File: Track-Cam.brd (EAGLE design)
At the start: 65 x 56 mm, 40 parts, among them IC1 STM32F042K6T, IC2 BD6211F, IC3 BD6211F, Q1 8MHz, X1 RASPI_BOARD_B+#_HC

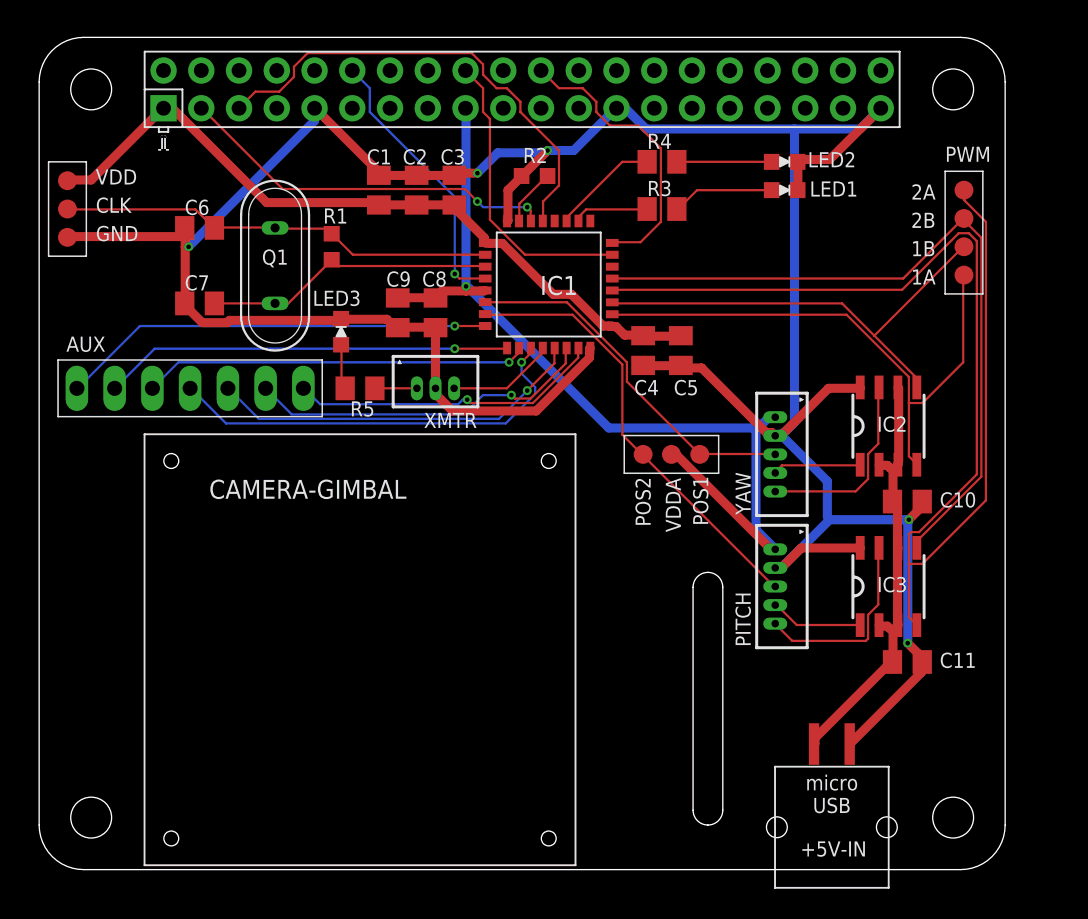
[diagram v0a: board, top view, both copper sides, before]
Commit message: enlarge pads
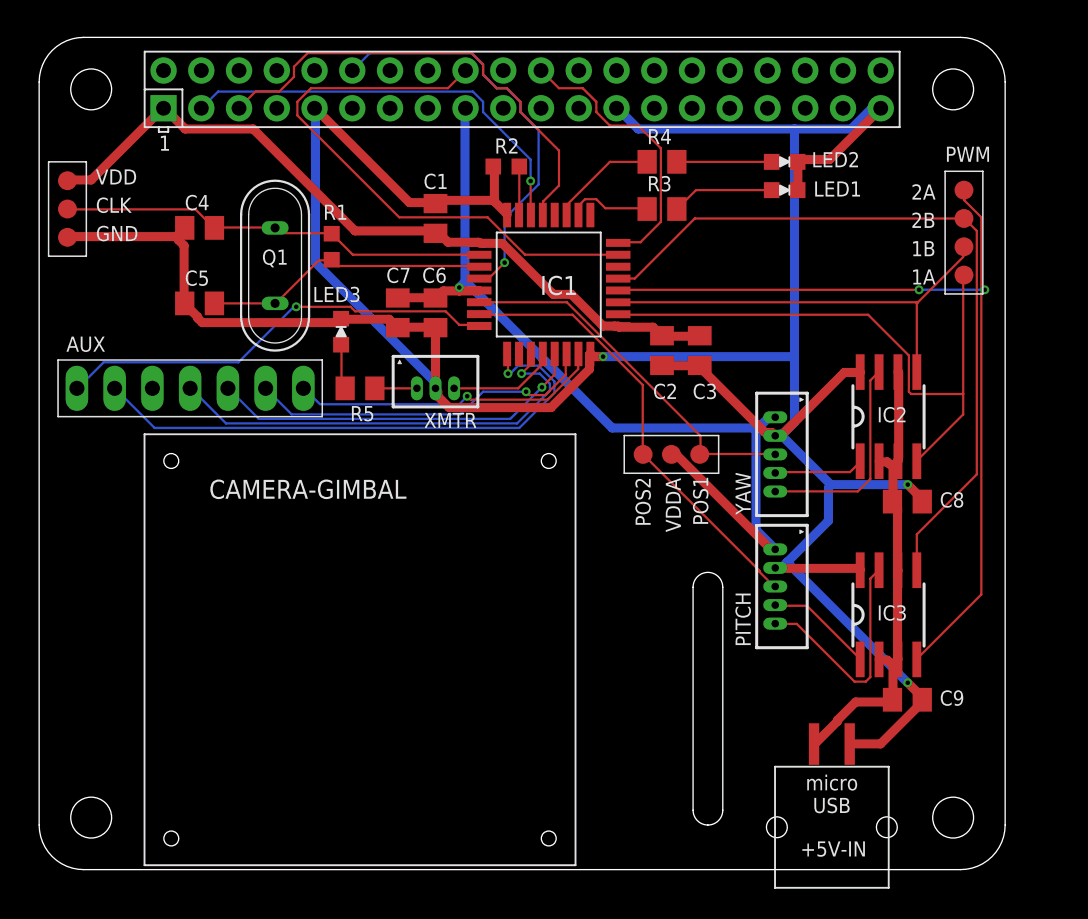
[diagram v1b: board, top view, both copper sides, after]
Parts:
- removed C10, C11: 10μ, gen-discrete:SMD2012
- C2: value 4.7μ -> 0.1μ
- C3: value 0.1μ -> 4.7μ
- C4: value 0.1μ -> 20p
- C5: value 4.7μ -> 20p
- C6: value 20p -> 10n
- C7: value 20p -> 1μ
- C9: value 1μ -> 10μ
- IC1: value STM32F042K6T -> STM32F042KT/M; device stm32:LQFP32 -> stm32:LQFP32-M
- IC2, IC3: value BD6211F -> BD6211F/M; device rohm-modified:SOP8 -> rohm-modified:SOP8/M
- moved C9 43.1 mm to (58.4, 11.4), turned to 0 degrees
- moved C8 34.2 mm to (58.4, 24.8), turned to 0 degrees
- moved C5 32.5 mm to (10.8, 38.1), turned to 0 degrees
- moved C4 31.0 mm to (10.8, 43.2), turned to 0 degrees
- moved C3 19.7 mm to (44.5, 34.9), turned to 270 degrees
- moved C2 19.7 mm to (41.9, 34.9), turned to 270 degrees
- moved C6 16.9 mm to (26.7, 37.5), turned to 270 degrees
- moved C7 13.4 mm to (24.1, 37.5), turned to 270 degrees
- moved C1 4.26 mm to (26.7, 43.8)
- moved R2 2.01 mm to (31.4, 47.3)
- moved IC3 1.91 mm to (57.1, 17.1)
- moved IC2 0.64 mm to (57.1, 30.5)
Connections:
- net PA2 renamed N$1
- net PA3 renamed N$2
- net PA5 renamed N$4
- net PA7 renamed N$5
- net PB0 renamed N$6
- net PB1 renamed N$7
- removed net PA4: AUX.3, IC1.10
- new net N$3: IC1.10
- net +3V3: now also C6.1, C7.1; no longer C8.1, C9.1
- net +5V: now also C8.1, C9.1; no longer C10.1, C11.1
- net GND: now also C4.1, C5.1, C6.2, C7.2; no longer C10.2, C11.2, C4.2, C5.2, C6.1, C7.1
- net OSC_IN: now also C4.2; no longer C6.2
- net OSC_OUT: now also C5.2; no longer C7.2
- net VDD: no longer C4.1, C5.1
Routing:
- net PA4: track 26.0 -> 0.00 mm, vias 1 -> 0
- net MOTOR2_F: track 83.1 -> 58.8 mm, vias 0 -> 2
- net SWDIO: track 19.9 -> 38.6 mm
- net GND: track 202.4 -> 213.5 mm, vias 5 -> 3
- net N$2: track 27.5 -> 37.6 mm
- net NRST: track 19.0 -> 28.0 mm
- net SDA: track 25.7 -> 28.7 mm, vias 2 -> 1
- net +5V: track 28.9 -> 31.2 mm
- net MOTOR2-: track 13.2 -> 15.6 mm
- net MOTOR1_F: track 38.5 -> 40.8 mm
- net MOTOR1_R: track 31.7 -> 29.9 mm
- net N$4: track 28.7 -> 30.3 mm
- net MOTOR1-: track 13.1 -> 14.2 mm
- net VDD: track 49.9 -> 50.9 mm
- net MOTOR2+: track 6.31 -> 7.27 mm
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
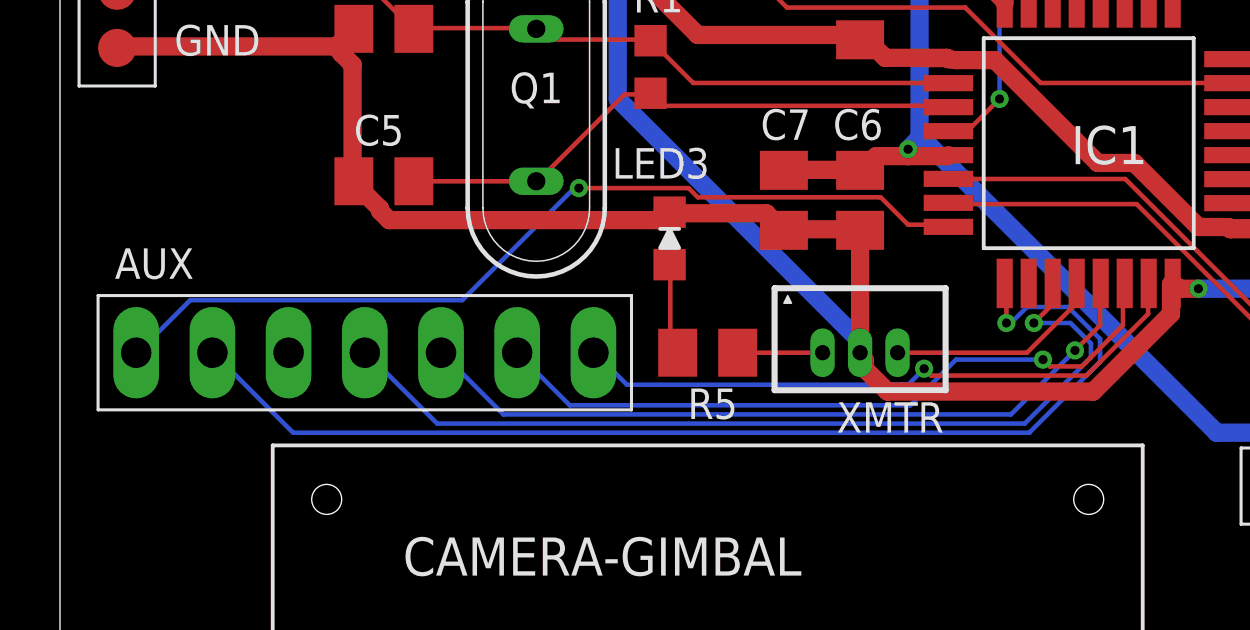
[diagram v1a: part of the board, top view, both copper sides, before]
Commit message: fix issue of unconnected path
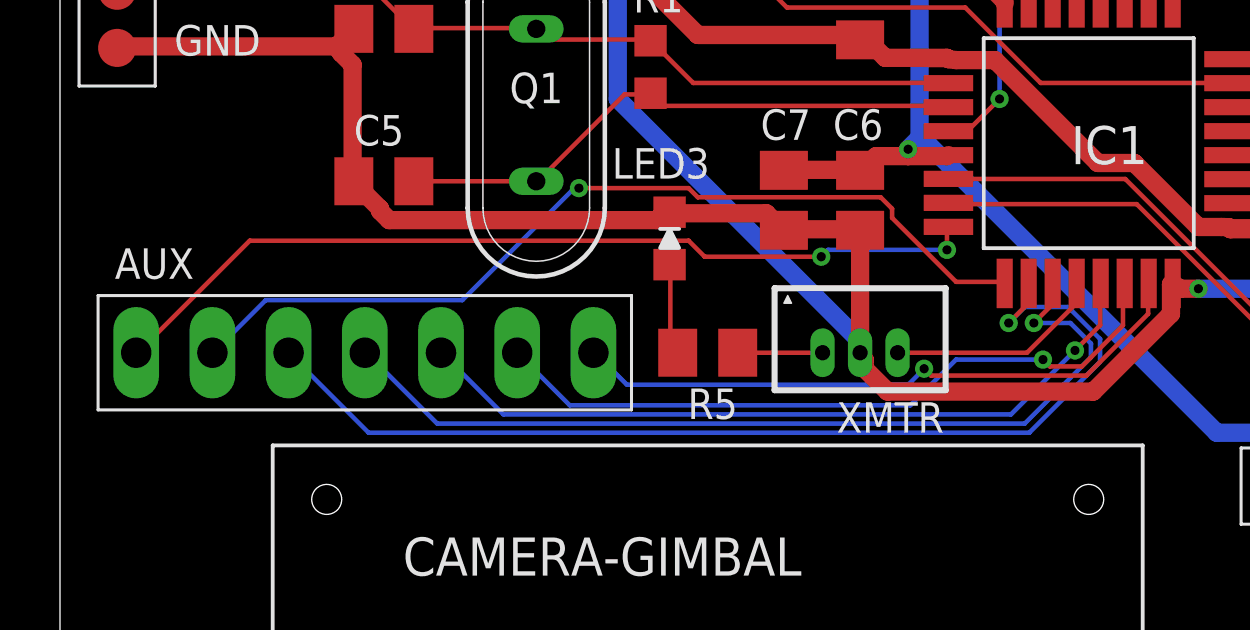
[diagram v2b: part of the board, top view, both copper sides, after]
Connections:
- net N$3: now also AUX.3
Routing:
- net N$3: track 0.00 -> 35.2 mm, vias 0 -> 1
- net N$2: track 37.6 -> 30.2 mm
- net N$1: track 29.9 -> 29.7 mm, vias 1 -> 2
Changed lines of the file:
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@@
 <contactref element="IC1" pad="8"/>
 <contactref element="AUX" pad="1"/>
-<wire x1="28.2702" y1="36.6522" x2="29.5656" y2="36.6522" width="0.1524" layer="1"/>
-<wire x1="27.3558" y1="37.5666" x2="28.2702" y2="36.6522" width="0.1524" layer="1"/>
+<wire x1="29.5656" y1="35.814" x2="29.5656" y2="36.576" width="0.1524" layer="1"/>
+<wire x1="25.6032" y1="35.814" x2="29.5656" y2="35.814" width="0.1524" layer="16"/>
+<wire x1="25.3746" y1="35.5854" x2="25.6032" y2="35.814" width="0.1524" layer="16"/>
+<wire x1="21.4884" y1="35.5854" x2="25.3746" y2="35.5854" width="0.1524" layer="1"/>
+<wire x1="20.955" y1="36.1188" x2="21.4884" y2="35.5854" width="0.1524" layer="1"/>
+<wire x1="6.3246" y1="36.1188" x2="20.955" y2="36.1188" width="0.1524" layer="1"/>
+<wire x1="2.5908" y1="32.385" x2="6.3246" y2="36.1188" width="0.1524" layer="1"/>
+<wire x1="29.5656" y1="36.576" x2="29.615" y2="36.58" width="0.1524" layer="1"/>
+<wire x1="2.5908" y1="32.385" x2="2.54" y2="32.385" width="0.1524" layer="1"/>
+<via x="29.5656" y="35.814" extent="1-16" drill="0.3048"/>
+<via x="25.3746" y="35.5854" extent="1-16" drill="0.3048"/>
+</signal>
+<signal name="N$2">
+<contactref element="IC1" pad="9"/>
+<contactref element="AUX" pad="2"/>
+<wire x1="29.8704" y1="34.7472" x2="31.4706" y2="34.7472" width="0.1524" layer="1"/>
+<wire x1="27.7368" y1="36.8808" x2="29.8704" y2="34.7472" width="0.1524" layer="1"/>
+<wire x1="27.7368" y1="37.1856" x2="27.7368" y2="36.8808" width="0.1524" layer="1"/>
+<wire x1="27.3558" y1="37.5666" x2="27.7368" y2="37.1856" width="0.1524" layer="1"/>
 <wire x1="21.2598" y1="37.5666" x2="27.3558" y2="37.5666" width="0.1524" layer="1"/>
 <wire x1="20.955" y1="37.8714" x2="21.2598" y2="37.5666" width="0.1524" layer="1"/>
@@
 <wire x1="17.145" y1="37.8714" x2="17.2974" y2="37.8714" width="0.1524" layer="16"/>
 <wire x1="13.4112" y1="34.1376" x2="17.145" y2="37.8714" width="0.1524" layer="16"/>
-<wire x1="4.3434" y1="34.1376" x2="13.4112" y2="34.1376" width="0.1524" layer="16"/>
-<wire x1="2.5908" y1="32.385" x2="4.3434" y2="34.1376" width="0.1524" layer="16"/>
-<wire x1="29.5656" y1="36.6522" x2="29.615" y2="36.58" width="0.1524" layer="1"/>
-<wire x1="2.5908" y1="32.385" x2="2.54" y2="32.385" width="0.1524" layer="16"/>
+<wire x1="6.858" y1="34.1376" x2="13.4112" y2="34.1376" width="0.1524" layer="16"/>
+<wire x1="5.1054" y1="32.385" x2="6.858" y2="34.1376" width="0.1524" layer="16"/>
+<wire x1="31.4706" y1="34.7472" x2="31.49" y2="34.695" width="0.1524" layer="1"/>
+<wire x1="5.1054" y1="32.385" x2="5.08" y2="32.385" width="0.1524" layer="16"/>
 <via x="17.2974" y="37.8714" extent="1-16" drill="0.3048"/>
-</signal>
-<signal name="N$2">
-<contactref element="IC1" pad="9"/>
-<contactref element="AUX" pad="2"/>
-<wire x1="31.5468" y1="33.3756" x2="31.5468" y2="34.671" width="0.1524" layer="1"/>
-<wire x1="31.6992" y1="33.3756" x2="31.5468" y2="33.3756" width="0.1524" layer="16"/>
-<wire x1="32.2326" y1="33.909" x2="31.6992" y2="33.3756" width="0.1524" layer="16"/>
-<wire x1="33.6042" y1="33.909" x2="32.2326" y2="33.909" width="0.1524" layer="16"/>
-<wire x1="34.671" y1="32.8422" x2="33.6042" y2="33.909" width="0.1524" layer="16"/>
-<wire x1="34.671" y1="32.0802" x2="34.671" y2="32.8422" width="0.1524" layer="16"/>
-<wire x1="32.3088" y1="29.718" x2="34.671" y2="32.0802" width="0.1524" layer="16"/>
-<wire x1="7.7724" y1="29.718" x2="32.3088" y2="29.718" width="0.1524" layer="16"/>
-<wire x1="5.1054" y1="32.385" x2="7.7724" y2="29.718" width="0.1524" layer="16"/>
-<wire x1="31.5468" y1="34.671" x2="31.49" y2="34.695" width="0.1524" layer="1"/>
-<wire x1="5.1054" y1="32.385" x2="5.08" y2="32.385" width="0.1524" layer="16"/>
-<via x="31.5468" y="33.3756" extent="1-16" drill="0.3048"/>
-</signal>
-<signal name="N$3">
-<contactref element="IC1" pad="10"/>
 </signal>
 <signal name="N$4">
@@
 <via x="28.8036" y="31.8516" extent="1-16" drill="0.3048"/>
 </signal>
+<signal name="N$3">
+<contactref element="IC1" pad="10"/>
+<contactref element="AUX" pad="3"/>
+<wire x1="32.2326" y1="33.9852" x2="32.2326" y2="34.671" width="0.1524" layer="1"/>
+<wire x1="31.623" y1="33.3756" x2="32.2326" y2="33.9852" width="0.1524" layer="1"/>
+<wire x1="32.1564" y1="33.909" x2="31.623" y2="33.3756" width="0.1524" layer="16"/>
+<wire x1="33.6042" y1="33.909" x2="32.1564" y2="33.909" width="0.1524" layer="16"/>
+<wire x1="34.671" y1="32.8422" x2="33.6042" y2="33.909" width="0.1524" layer="16"/>
+<wire x1="34.671" y1="32.0802" x2="34.671" y2="32.8422" width="0.1524" layer="16"/>
+<wire x1="32.3088" y1="29.718" x2="34.671" y2="32.0802" width="0.1524" layer="16"/>
+<wire x1="10.287" y1="29.718" x2="32.3088" y2="29.718" width="0.1524" layer="16"/>
+<wire x1="7.62" y1="32.385" x2="10.287" y2="29.718" width="0.1524" layer="16"/>
+<wire x1="32.2326" y1="34.671" x2="32.29" y2="34.695" width="0.1524" layer="1"/>
+<via x="31.623" y="33.3756" extent="1-16" drill="0.3048"/>
+</signal>
 </signals>

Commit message: add polygon net
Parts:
- +5V-IN: value MRUSB-2B-D14NI-S306 -> MRUSB-2B-D14NI-S306/M; device connector:MICRO-USB-POWER -> connector:MICRO-USB-POWER/M
- moved C8 1.91 mm to (56.5, 24.8), turned to 180 degrees
- moved C9 1.91 mm to (56.5, 11.4), turned to 180 degrees
- moved CLK 1.91 mm to (3.81, 44.5)
- moved GND 1.91 mm to (3.81, 42.5)
- moved VDD 1.91 mm to (3.81, 46.4)
- renumbered Q1 to XT1
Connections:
- net N$1 renamed PA2
- net N$2 renamed PA3
- net N$3 renamed PA4
- net N$4 renamed PA5
- net N$5 renamed PA7
- net N$6 renamed PB0
- net N$7 renamed PB1
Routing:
- net GND: track 213.5 -> 188.2 mm, vias 3 -> 10
- net VDD: track 50.9 -> 42.4 mm
- net MOTOR2_R: track 50.7 -> 55.9 mm
- net +5V: track 31.2 -> 35.0 mm
- net OSC_IN: track 29.0 -> 27.1 mm
- net MOTOR2_F: track 58.8 -> 60.6 mm, vias 2 -> 0
- net +3V3: vias 1 -> 3
- added copper zone on layer 1, net +3V3
- added copper zone on layer 16, net +3V3
- added copper zone on layer 1, net +5V
- added copper zone on layer 1, net GND
- added copper zone on layer 16, net GND
- added copper zone on layer 1, net VDD

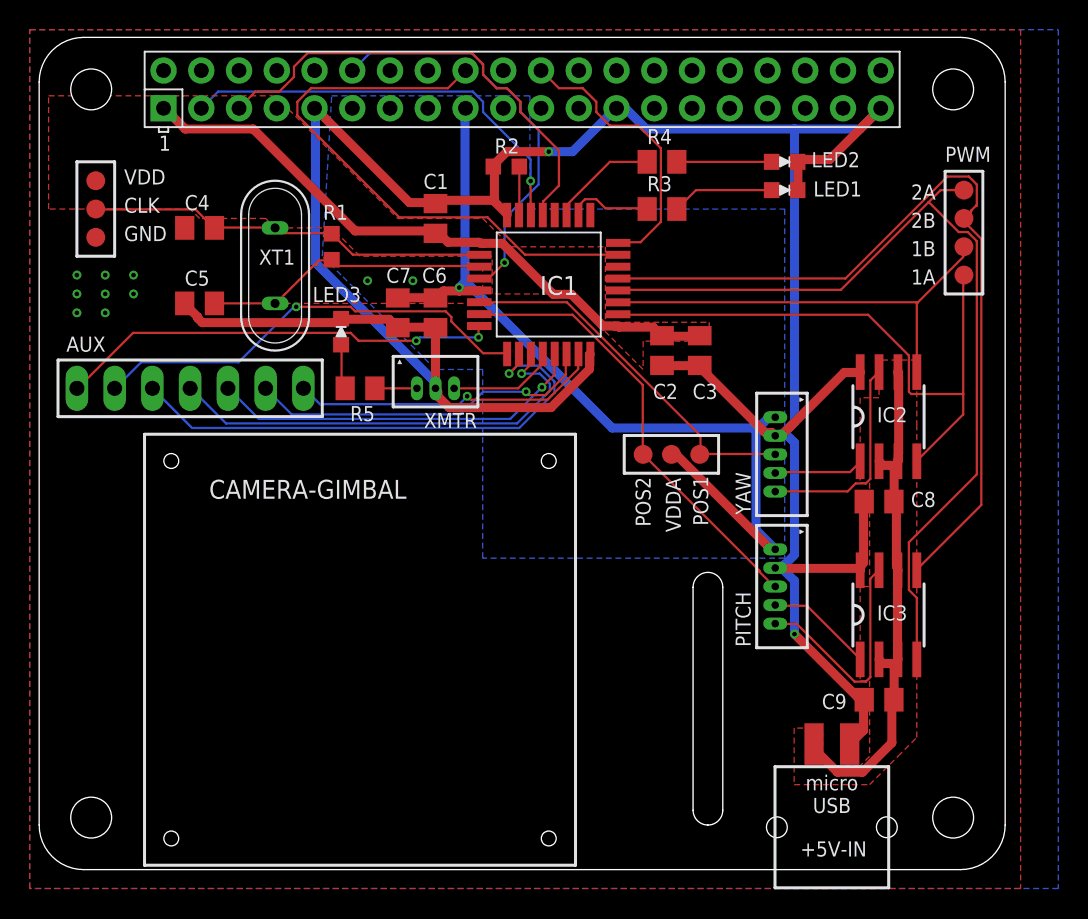
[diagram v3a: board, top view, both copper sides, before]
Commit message: replaced components to confirm to actual gimbal size
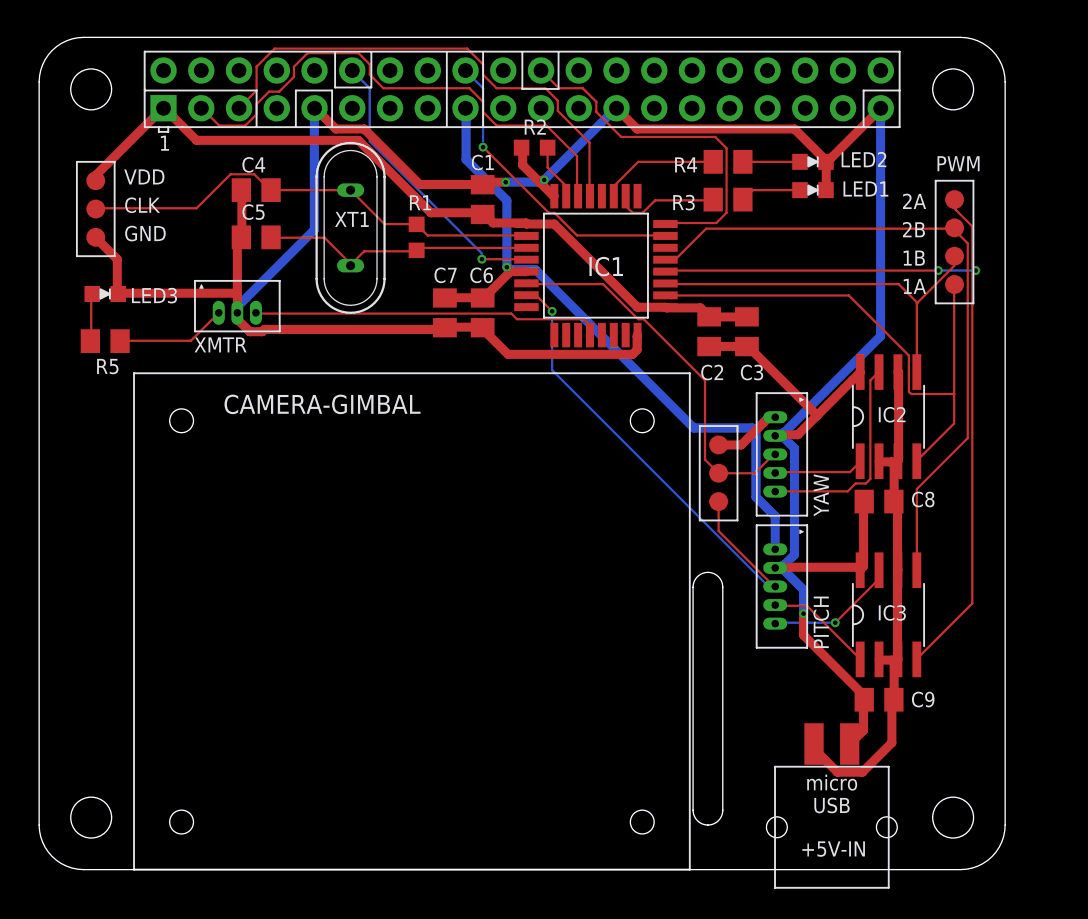
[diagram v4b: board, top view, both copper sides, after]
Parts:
- removed AUX: AUX PORT, connector:1X07/NS
- moved R5 17.4 mm to (4.45, 35.6)
- moved LED3 16.1 mm to (4.45, 38.7), turned to 0 degrees
- moved XMTR 14.3 mm to (13.3, 37.5)
- moved POS2 5.99 mm to (45.7, 24.8)
- moved C5 5.85 mm to (14.6, 42.5)
- moved R1 5.75 mm to (25.4, 42.5)
- moved XT1 5.68 mm to (21.0, 43.2)
- moved C4 4.58 mm to (14.6, 45.7)
- moved R3 4.49 mm to (46.4, 45.1)
- moved R4 4.45 mm to (46.4, 47.6)
- moved CAMERA-GIMBAL 3.98 mm to (25.1, 16.7)
- moved C2 3.42 mm to (45.1, 36.2)
- moved IC1 3.42 mm to (37.5, 40.6)
- moved C1 3.42 mm to (29.8, 45.1)
- moved C3 3.42 mm to (47.6, 36.2)
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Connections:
- removed net PA2: AUX.1, IC1.8
- removed net PA3: AUX.2, IC1.9
- removed net PA4: AUX.3, IC1.10
- removed net PA5: AUX.4, IC1.11
- removed net PA7: AUX.5, IC1.13
- removed net PB0: AUX.6, IC1.14
- removed net PB1: AUX.7, IC1.15
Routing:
- net PA4: track 35.2 -> 0.00 mm, vias 1 -> 0
- net PA5: track 30.3 -> 0.00 mm, vias 1 -> 0
- net PA3: track 30.2 -> 0.00 mm, vias 1 -> 0
- net PA2: track 29.7 -> 0.00 mm, vias 2 -> 0
- net PA7: track 25.5 -> 0.00 mm, vias 1 -> 0
- net PB0: track 23.6 -> 0.00 mm, vias 1 -> 0
- net PB1: track 21.1 -> 0.00 mm, vias 1 -> 0
- net SWDIO: track 38.6 -> 20.4 mm, vias 0 -> 1
- net TRAINER: track 7.32 -> 23.5 mm
- net MOTOR2_R: track 55.9 -> 45.2 mm
- net VDD: track 42.4 -> 51.8 mm
- net NRST: track 28.0 -> 19.3 mm
- net GND: track 188.2 -> 196.2 mm, vias 10 -> 3
- net +3V3: track 61.7 -> 54.5 mm, vias 3 -> 1
- net MOTOR2-: track 15.6 -> 8.86 mm, vias 0 -> 1
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- removed copper zone on layer 1, net +3V3
- removed copper zone on layer 16, net +3V3
- removed copper zone on layer 1, net +5V
- removed copper zone on layer 1, net GND
- removed copper zone on layer 16, net GND
- removed copper zone on layer 1, net VDD
